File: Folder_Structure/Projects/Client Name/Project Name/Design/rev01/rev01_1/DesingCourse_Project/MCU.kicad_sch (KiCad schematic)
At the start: 0 parts

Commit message: Update 3
MCU SCH done
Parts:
- added C1: 10u, symbol Device:C
- added C10, C9: 2u2, symbol Device:C
- added C11: 1u, symbol Device:C
- added C12, C15, C16, C17, C2, C3, C4, C5, C6, C7, C8: 100n, symbol Device:C
- added C13, C14: 10p, symbol Device:C
- added D1, D3: LED_G, symbol Device:LED
- added D2: LED_R, symbol Device:LED
- added FB1: FerriteBead, symbol Device:FerriteBead
- added J1: Conn_01x06_Pin, symbol Connector:Conn_01x06_Pin
- added J2: Conn_01x03_Pin, symbol Connector:Conn_01x03_Pin
- added J3: Conn_01x08_Pin, symbol Connector:Conn_01x08_Pin
- added R1, R2, R3: 0R, symbol Device:R
- added R10: 39K, symbol Device:R
- added R4, R5, R8: 1k, symbol Device:R
- added R6: 2k2, symbol Device:R
- added R7, R9: 2K2, symbol Device:R
- added SW1: SW_DIP_x01, symbol Switch:SW_DIP_x01
- added TH1: 10k, symbol Device:Thermistor_NTC
- added U1: STM32F405RGTx, Package_QFP:LQFP-64_10x10mm_P0.5mm, symbol MCU_ST_STM32F4:STM32F405RGTx
- added Y1: 8MHz, symbol Device:Crystal
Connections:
- new net: J2.1 (Pin_1), R6.2
- new net: D2.2 (A), R5.1
- new net: D3.2 (A), R8.1
- new net: D1.2 (A), R4.1
- new net +VDC: R10.1
- new net ADC_TEMP: R7.1, TH1.2, U1.17 (PA3)
- new net AN_IN: C17.1, R10.2, R9.1, U1.10 (PC2)
- new net BOOT_P: R1.2, U1.60 (BOOT0)
- new net BR_SD1: U1.27 (PB1)
- new net BR_SD2: U1.26 (PB0)
- new net CAN_RX: U1.61 (PB8)
- new net CAN_TX: U1.62 (PB9)
- new net DC_CAL: U1.33 (PB12)
- new net EN_GATE: U1.51 (PC10)
- new net FAULT: U1.53 (PC12)
- new net GND: C1.2, C10.2, C11.2, C12.2, C13.2, C14.2, C15.2, C16.2, C17.2, C2.2, C3.2, C4.2, C5.2, C6.2, C7.2, C8.2, C9.2, D1.1 (K), D2.1 (K), D3.1 (K), J1.3 (Pin_3), J2.2 (Pin_2), J3.3 (Pin_3), J3.8 (Pin_8), R7.2, R9.2, SW1.1, U1.12 (VSSA), U1.18 (VSS), U1.63 (VSS)
- new net H1: U1.43 (PA10)
- new net H2: U1.42 (PA9)
- new net H3: U1.41 (PA8)
- new net HALL1_OUT: U1.58 (PB6)
- new net HALL2_OUT: U1.59 (PB7)
- new net HALL3_OUT: U1.52 (PC11)
- new net L1: U1.36 (PB15)
- new net L2: U1.35 (PB14)
- new net L3: U1.34 (PB13)
- new net LED_GREEN: R4.2, U1.24 (PC4)
- new net LED_RED: R5.2, U1.25 (PC5)
- new net MISO_ADC_EXT2: J3.7 (Pin_7), U1.22 (PA6)
- new net NRST: C8.1, J1.5 (Pin_5), SW1.2, U1.7 (NRST)
- new net P3V3: C1.1, C16.1, C2.1, C3.1, C4.1, C5.1, C6.1, C7.1, FB1.2, J1.1 (Pin_1), J3.2 (Pin_2), R1.1, R8.2, TH1.1, U1.1 (VBAT), U1.19 (VDD), U1.32 (VDD), U1.48 (VDD), U1.64 (VDD)
- new net P3V3_A: C11.1, C12.1, FB1.1, U1.13 (VDDA)
- new net P5V: J2.3 (Pin_3), J3.1 (Pin_1)
- new net PH0_P: R2.2, U1.5 (PH0)
- new net PH1_P: R3.2, U1.6 (PH1)
- new net PH_0: C13.1, R2.1, Y1.1
- new net PH_1: C14.1, R3.1, Y1.2
- new net RX_SDA_NSS: J3.5 (Pin_5), U1.20 (PA4), U1.30 (PB11), U1.37 (PC6)
- new net SCK_ADC_EXT: J3.4 (Pin_4), U1.21 (PA5)
- new net SENS1: U1.16 (PA2)
- new net SENS2: U1.15 (PA1)
- new net SENS3: U1.14 (PA0)
- new net SERVO: C15.1, R6.1, U1.57 (PB5)
- new net SWCLK: J1.2 (Pin_2), U1.49 (PA14)
- new net SWDIO: J1.4 (Pin_4), U1.46 (PA13)
- new net TEMP_MOTOR: U1.8 (PC0)
- new net TX_SCL_MOSI: J3.6 (Pin_6), U1.23 (PA7), U1.29 (PB10), U1.38 (PC7)
- new net USB_N: U1.44 (PA11)
- new net USB_P: U1.45 (PA12)
- new net VCAP_1: C9.1, U1.31 (VCAP_1)
- new net VCAP_2: C10.1, U1.47 (VCAP_2)
- no-connect marks 0 -> 13
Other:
- note added: "100nF Decoupling caps. Place as close as possible to each pin."
- note added: "COMMUNICATION"
- note added: "MCU"
- note added: "NRST internally pulled-up."
- note added: "NTC THERMISTOR"
- note added: "PROGRAMMING / DEBUG"
- note added: "SERVO"
- note added: "SUBSTITUTE R6 WITH 100R IF USED AS SERVO OUTPUT"
- note added: "VOLTAGE_DIVIDER"
- note added: "WHEN: VDC = 60V => AN_IN = 3V204"

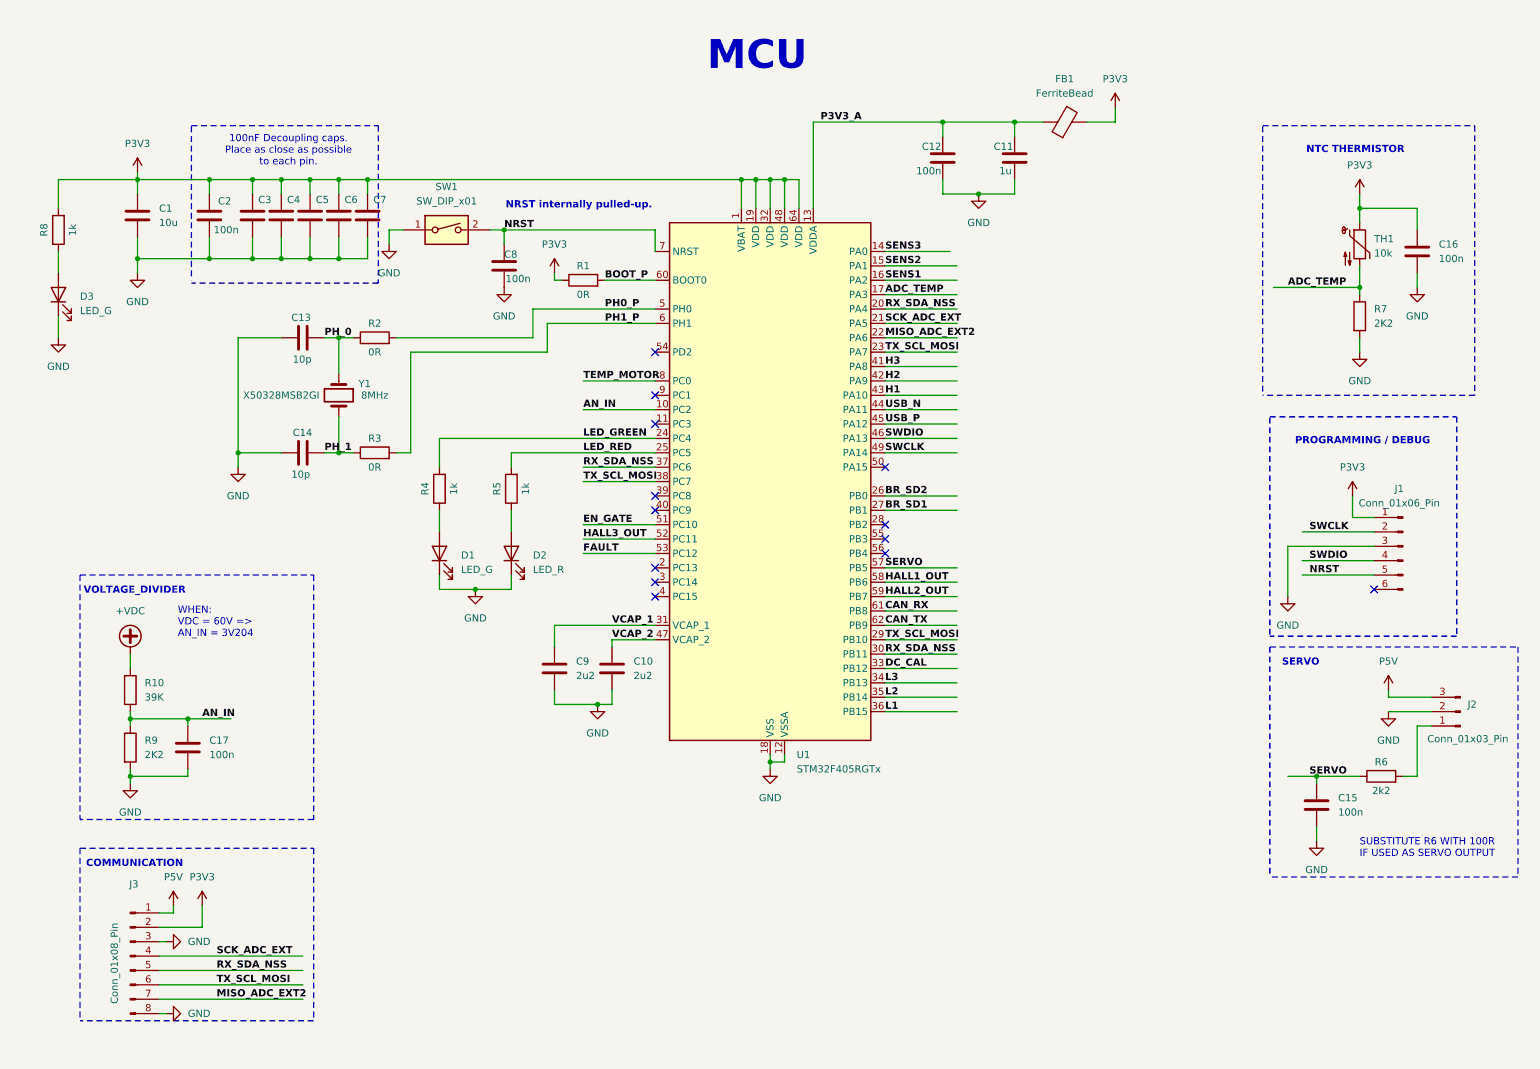
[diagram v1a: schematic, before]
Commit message: Update 4
Finish the MOSFET DRIVE page
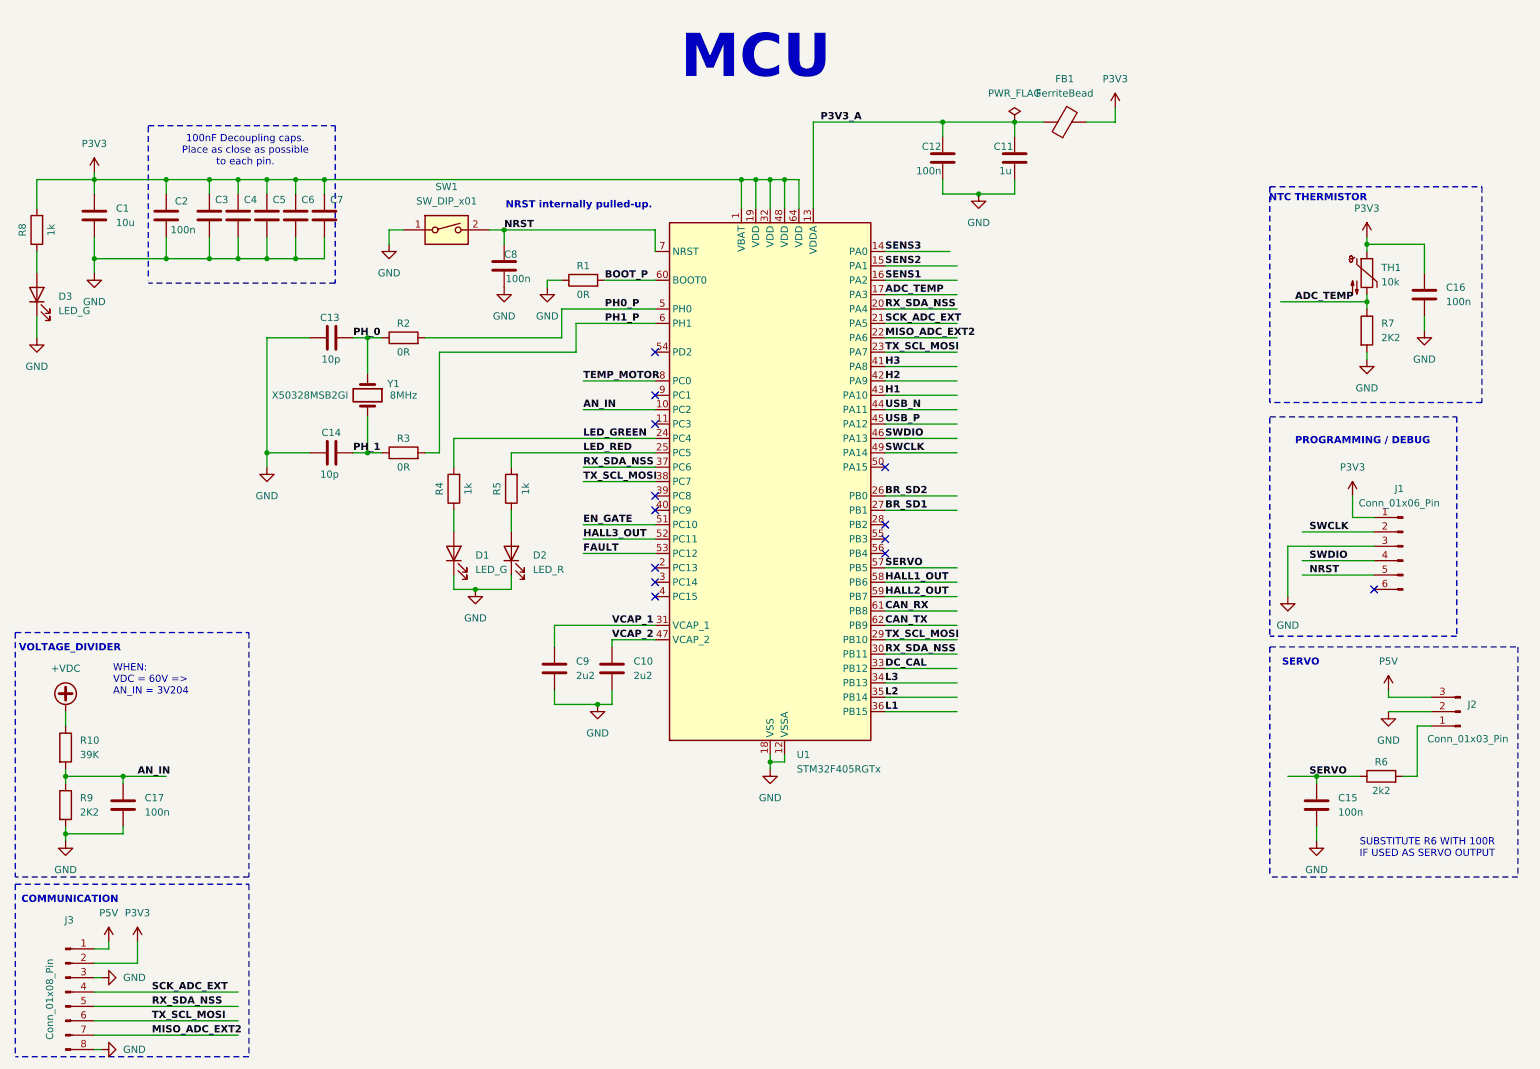
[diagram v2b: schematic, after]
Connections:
- net GND: now also R1.1
- net P3V3: no longer R1.1
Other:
- moved on the sheet: C1, C13, C14, C16, C17, C2, C3, C4, C5, C6, C7, D1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

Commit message: Update 6
SCH and LIB for MOSFET page done, missing passive components
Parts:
- Y1: MPN (none) -> X50328MSB2GI; PN X50328MSB2GI -> (none)
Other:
- company: (none) -> Integro Consulting AB
- title: (none) -> PCB Mastery Project
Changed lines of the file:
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@@
 	(generator_version "9.0")
 	(paper "A4")
+	(title_block
+		(title "PCB Mastery Project")
+		(date "2026-01-27")
+		(rev "001")
+		(company "Integro Consulting AB")
+		(comment 1 "TBD")
+		(comment 2 "TBD")
+		(comment 3 "TBD")
+		(comment 4 "Josue Godinez")
+	)
 	(text "PROGRAMMING / DEBUG"
 		(exclude_from_sim no)
@@
 			)
 		)
-		(property "PN" "X50328MSB2GI"
+		(property "MPN" "X50328MSB2GI"
 			(at 66.04 80.01 90)
 			(effects

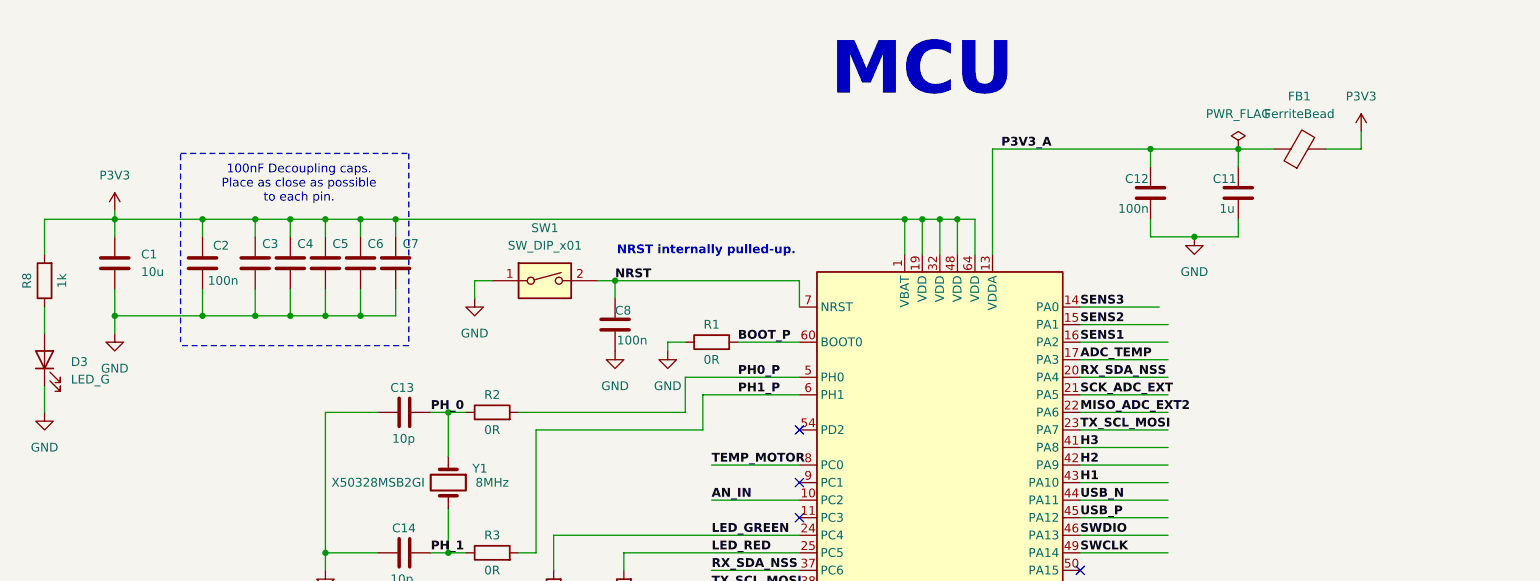
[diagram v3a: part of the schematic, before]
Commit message: Update 8
Page 1 finished, INPUT finished, Start of USB-C
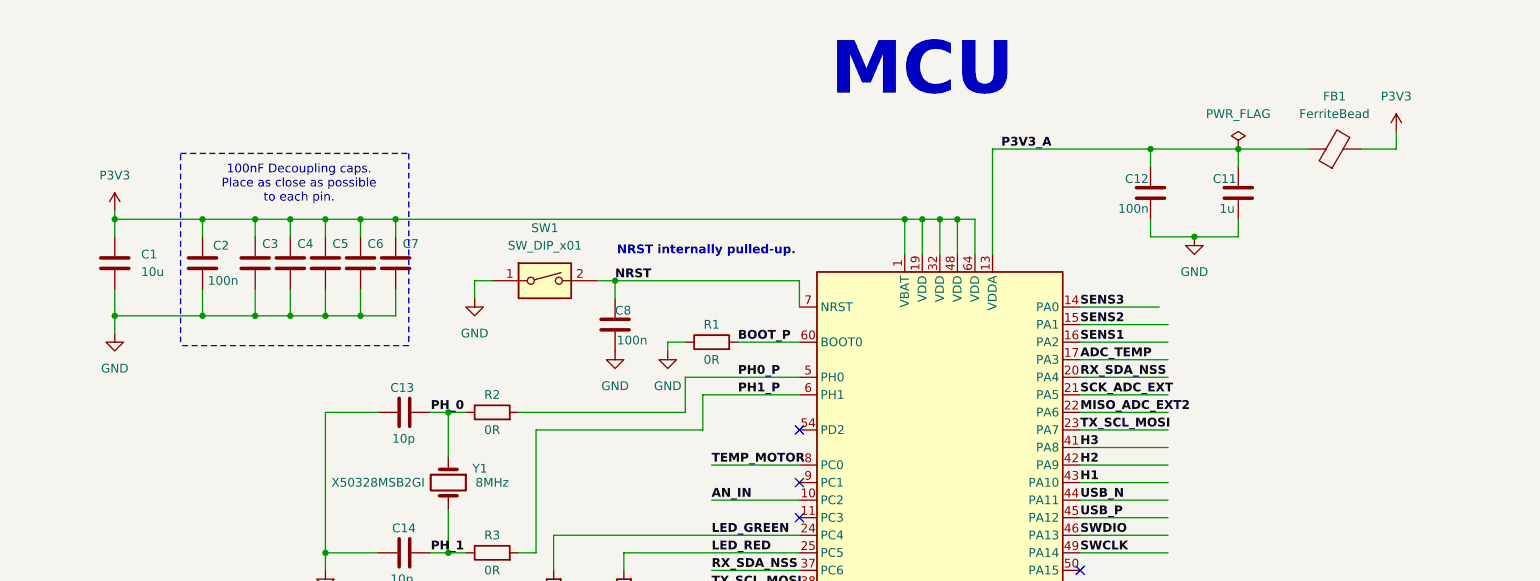
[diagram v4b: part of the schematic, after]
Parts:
- removed D3: LED_G, symbol Device:LED
- removed R8: 1k, symbol Device:R
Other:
- moved on the sheet: FB1

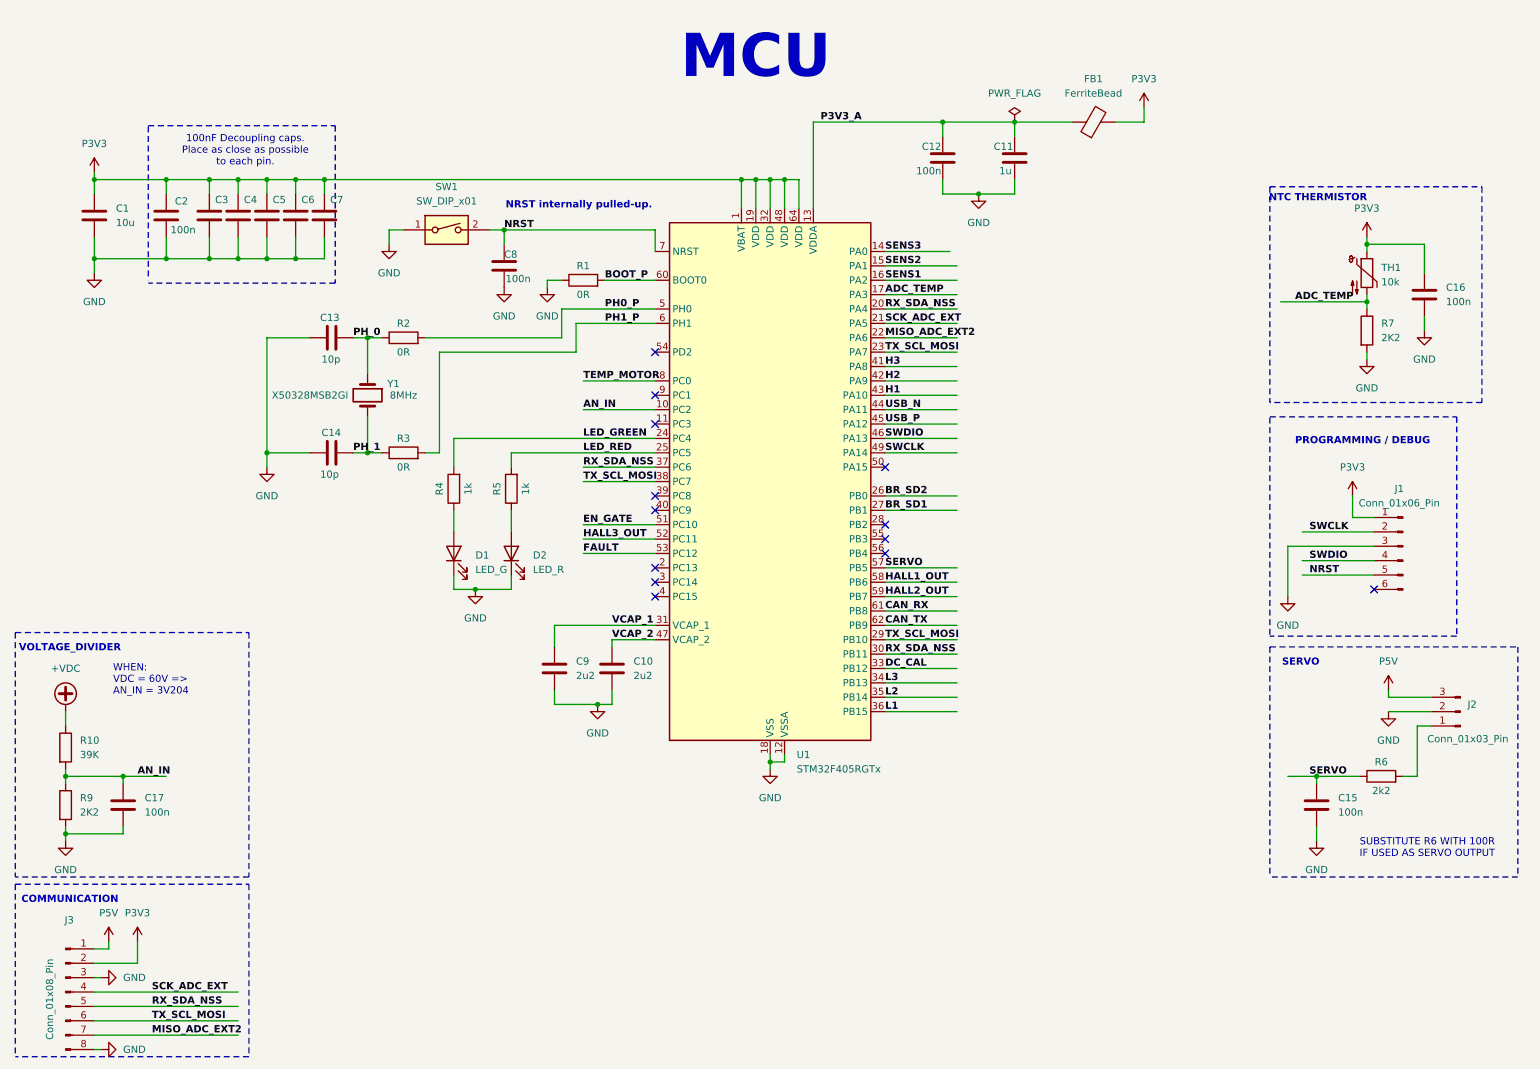
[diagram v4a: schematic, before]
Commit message: Update 9
USC-C & STEP_DOWN are DONE // MCU missing TVS diodes on P3V3 & P5V
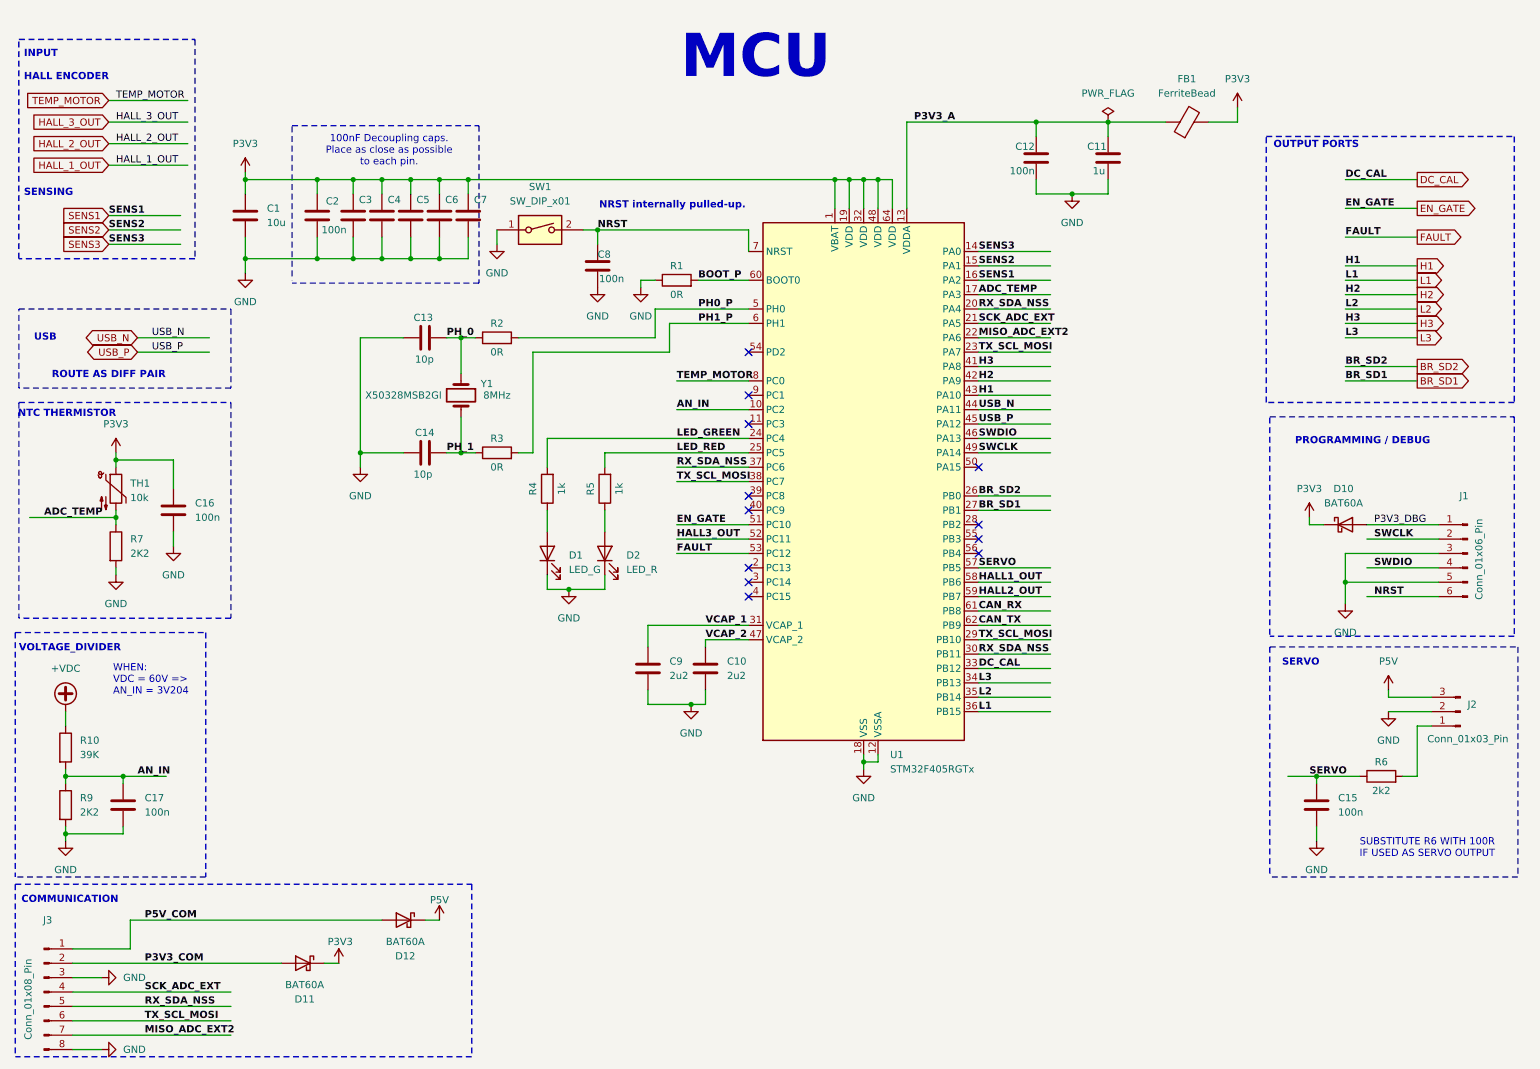
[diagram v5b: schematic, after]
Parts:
- added D10, D11, D12: BAT60A, Diode_SMD:D_SOD-323, symbol Diode:BAT60A
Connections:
- net GND: now also J1.5 (Pin_5)
- net NRST: now also J1.6 (Pin_6); no longer J1.5 (Pin_5)
- net P3V3: now also D10.1 (K), D11.1 (K); no longer J1.1 (Pin_1), J3.2 (Pin_2)
- net P5V: now also D12.1 (K); no longer J3.1 (Pin_1)
- new net P3V3_COM: D11.2 (A), J3.2 (Pin_2)
- new net P3V3_DBG: D10.2 (A), J1.1 (Pin_1)
- new net P5V_COM: D12.2 (A), J3.1 (Pin_1)
- no-connect marks 13 -> 12
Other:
- note added: "INPUT HALL ENCODER SENSING"
- note added: "OUTPUT PORTS"
- note added: "ROUTE AS DIFF PAIR"
- note added: "USB"
- moved on the sheet: C1, C10, C11, C12, C13, C14, C16, C2, C3, C4, C5, C6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
